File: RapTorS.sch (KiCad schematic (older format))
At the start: 23 parts, among them J1 TestPoint, J2 TestPoint, J3 TestPoint, J4 TestPoint, J5 TestPoint

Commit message: annotate schematic
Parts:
- removed C?: C, symbol RapTorS-rescue:C-device
- gave numbers to parts that had none: 16
- renumbered 0.1uF to 0.1uF1

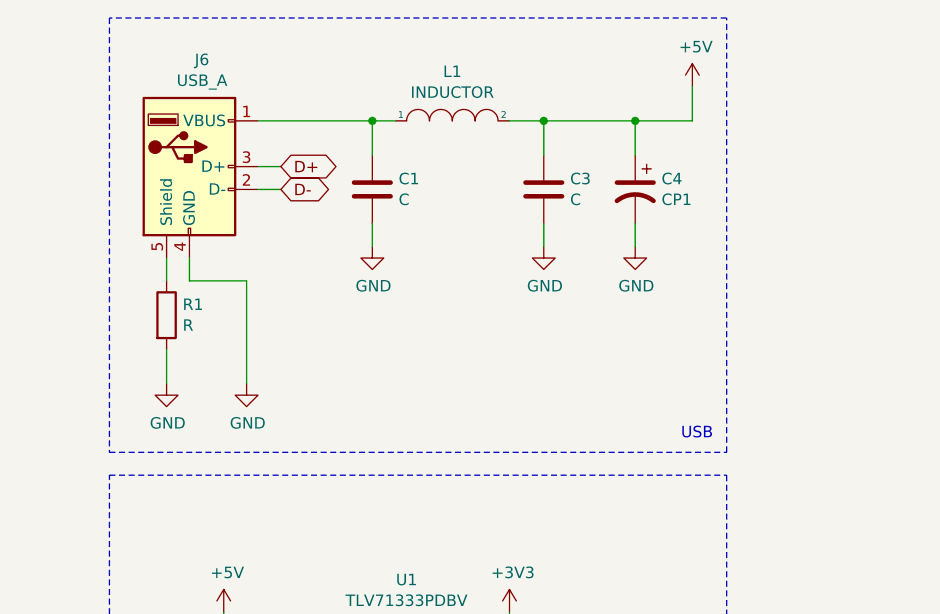
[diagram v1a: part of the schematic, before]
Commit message: set values for USB block
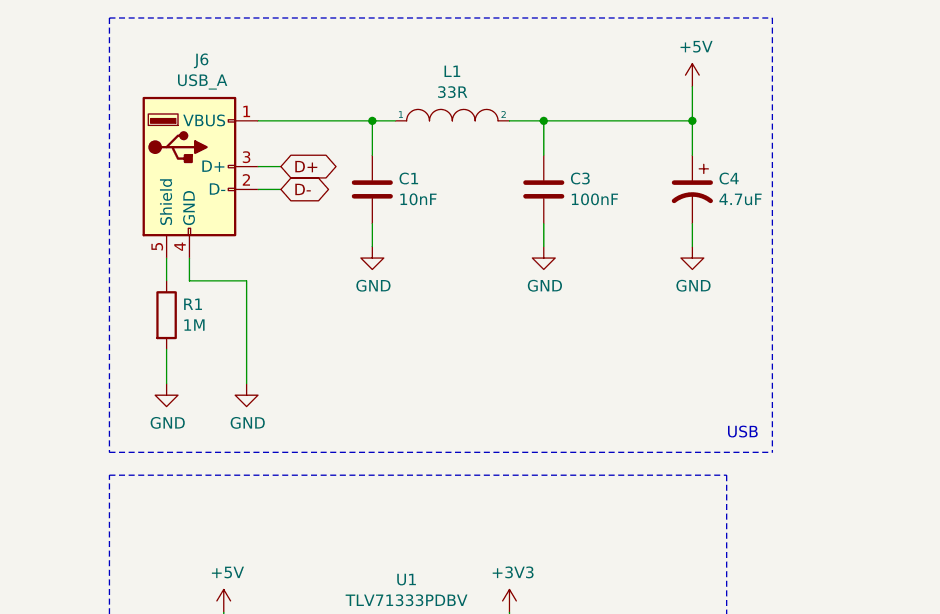
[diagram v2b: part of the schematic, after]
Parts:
- C1: value C -> 10nF
- C3: value C -> 100nF
- C4: value CP1 -> 4.7uF
- L1: value INDUCTOR -> 33R; footprint (none) -> Inductors_SMD:L_0805; Comment (none) -> Ferrite bead
- R1: value R -> 1M; footprint (none) -> Resistors_SMD:R_0805
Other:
- moved on the sheet: C4
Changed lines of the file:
@@
 P 2900 1550
 F 0 "C3" H 3015 1596 50  0000 L CNN
-F 1 "C" H 3015 1505 50  0000 L CNN
+F 1 "100nF" H 3015 1505 50  0000 L CNN
 F 2 "" H 2938 1400 50  0001 C CNN
 F 3 "" H 2900 1550 50  0001 C CNN
@@
 P 1250 2100
 F 0 "R1" H 1320 2146 50  0000 L CNN
-F 1 "R" H 1320 2055 50  0000 L CNN
-F 2 "" V 1180 2100 50  0001 C CNN
+F 1 "1M" H 1320 2055 50  0000 L CNN
+F 2 "Resistors_SMD:R_0805" V 1180 2100 50  0001 C CNN
 F 3 "" H 1250 2100 50  0001 C CNN
 	1    1250 2100
@@
 P 2500 1250
 F 0 "L1" H 2500 1465 50  0000 C CNN
-F 1 "INDUCTOR" H 2500 1374 50  0000 C CNN
-F 2 "" H 2500 1250 50  0001 C CNN
+F 1 "33R" H 2500 1374 50  0000 C CNN
+F 2 "Inductors_SMD:L_0805" H 2500 1250 50  0001 C CNN
 F 3 "" H 2500 1250 50  0001 C CNN
+F 4 "Ferrite bead" H 2500 1250 50  0001 C CNN "Comment"
 	1    2500 1250
 	1    0    0    -1
@@
 P 2150 1550
 F 0 "C1" H 2265 1596 50  0000 L CNN
-F 1 "C" H 2265 1505 50  0000 L CNN
+F 1 "10nF" H 2265 1505 50  0000 L CNN
 F 2 "" H 2188 1400 50  0001 C CNN
 F 3 "" H 2150 1550 50  0001 C CNN
@@
 L RapTorS-rescue:CP1-device C4
 U 1 1 5B63038C
-P 3300 1550
-F 0 "C4" H 3185 1596 50  0000 R CNN
-F 1 "CP1" H 3185 1505 50  0000 R CNN
-F 2 "" H 3300 1550 50  0001 C CNN
-F 3 "" H 3300 1550 50  0001 C CNN
-	1    3300 1550
+P 3550 1550
+F 0 "C4" H 3435 1596 50  0000 R CNN
+F 1 "4.7uF" H 3435 1505 50  0000 R CNN
+F 2 "" H 3550 1550 50  0001 C CNN
+F 3 "" H 3550 1550 50  0001 C CNN
+	1    3550 1550
 	-1   0    0    -1
 $EndComp
@@
 	2900 1250 2900 1400
 Wire Wire Line
-	2900 1250 3300 1250
-Wire Wire Line
-	3300 1250 3300 1400
+	2900 1250 3550 1250
+Wire Wire Line
+	3550 1250 3550 1400
 Connection ~ 2900 1250
 $Comp
@@
 Wire Wire Line
 	3550 1100 3550 1250
-Wire Wire Line
-	3550 1250 3300 1250
-Connection ~ 3300 1250
+Connection ~ 3550 1250
 $Comp
 L power:GND #PWR06
@@
 L power:GND #PWR012
 U 1 1 5B63068F
-P 3300 1800
-F 0 "#PWR012" H 3300 1550 50  0001 C CNN
-F 1 "GND" H 3305 1627 50  0000 C CNN
-F 2 "" H 3300 1800 50  0001 C CNN
-F 3 "" H 3300 1800 50  0001 C CNN
-	1    3300 1800
+P 3550 1800
+F 0 "#PWR012" H 3550 1550 50  0001 C CNN
+F 1 "GND" H 3555 1627 50  0000 C CNN
+F 2 "" H 3550 1800 50  0001 C CNN
+F 3 "" H 3550 1800 50  0001 C CNN
+	1    3550 1800
 	1    0    0    -1
 $EndComp
@@
 	2900 1700 2900 1800
 Wire Wire Line
-	3300 1700 3300 1800
+	3550 1700 3550 1800
 $Comp
 L power:GND #PWR01
@@
 D-
 Wire Notes Line
-	1000 2700 3700 2700
-Wire Notes Line
-	3700 2700 3700 800
-Wire Notes Line
-	3700 800  1000 800
-Wire Notes Line
 	1000 800  1000 2700
-Text Notes 3500 2650 0    50   ~ 0
+Text Notes 3700 2650 0    50   ~ 0
 USB
 $Comp
@@
 Text Notes 5850 4600 0    50   ~ 0
 PROG
+Wire Notes Line
+	3900 800  3900 2700
+Wire Notes Line
+	1000 2700 3900 2700
+Wire Notes Line
+	1000 800  3900 800
 $EndSCHEMATC

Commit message: set values for CPU block
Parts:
- C5: value C -> 100nF; footprint (none) -> Capacitors_SMD:C_0805
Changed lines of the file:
@@
 P 5400 1700
 F 0 "C5" H 5515 1746 50  0000 L CNN
-F 1 "C" H 5515 1655 50  0000 L CNN
-F 2 "" H 5438 1550 50  0001 C CNN
+F 1 "100nF" H 5515 1655 50  0000 L CNN
+F 2 "Capacitors_SMD:C_0805" H 5438 1550 50  0001 C CNN
 F 3 "" H 5400 1700 50  0001 C CNN
 	1    5400 1700

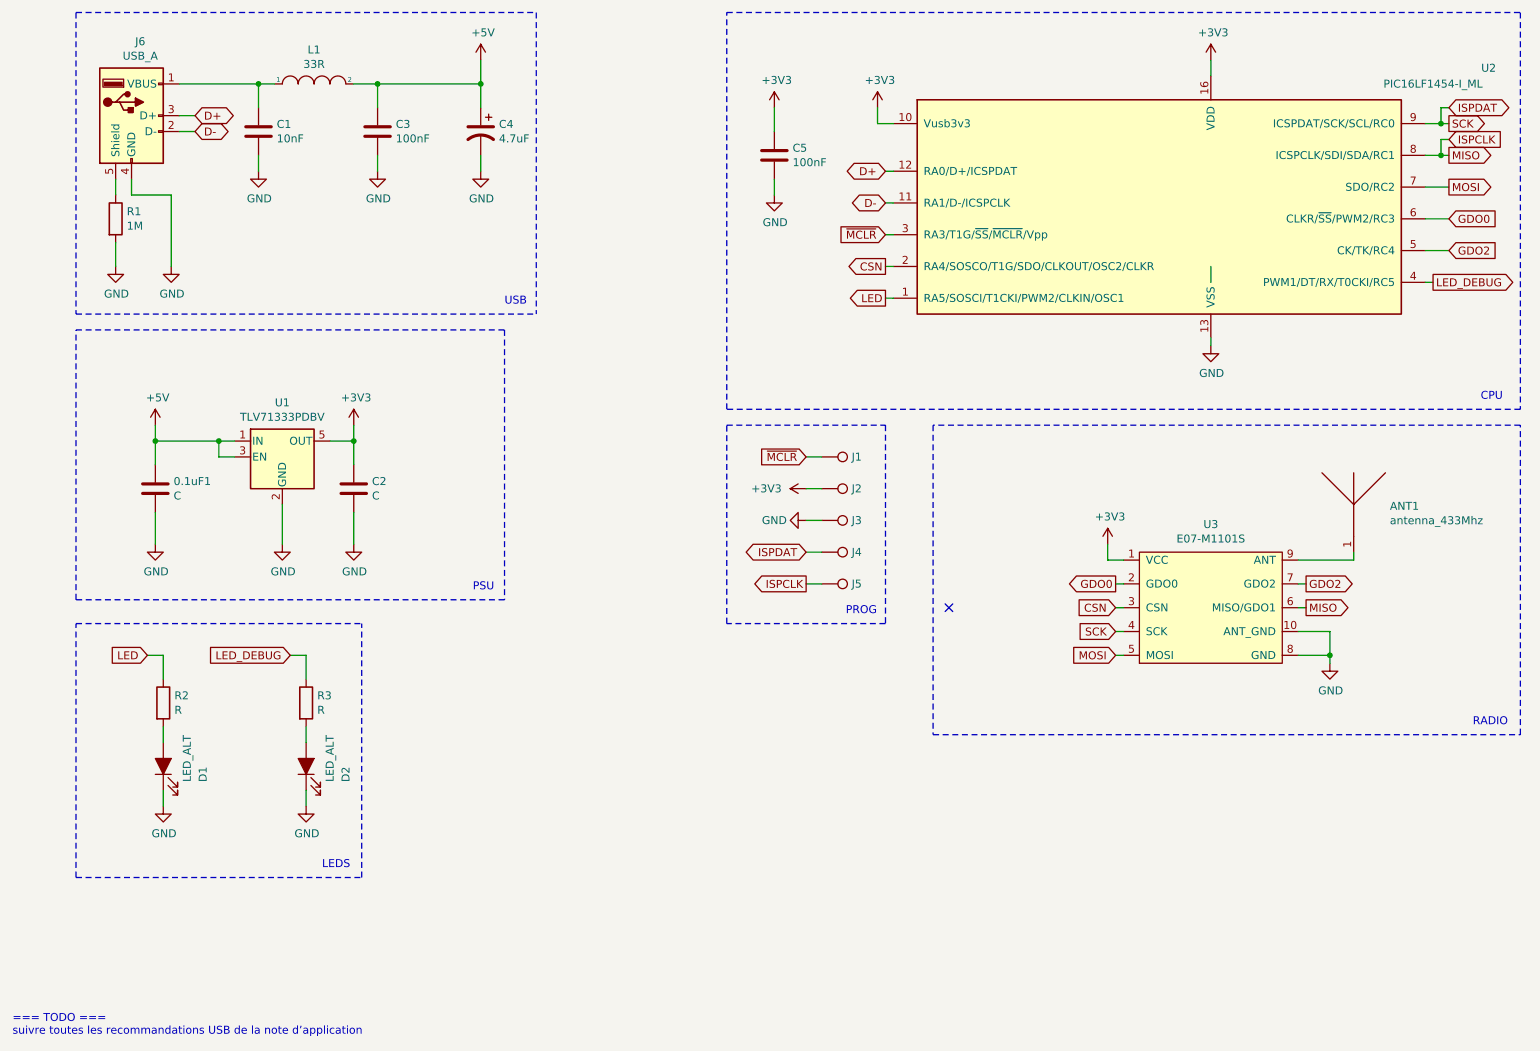
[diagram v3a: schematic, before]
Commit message: set values for PSU block
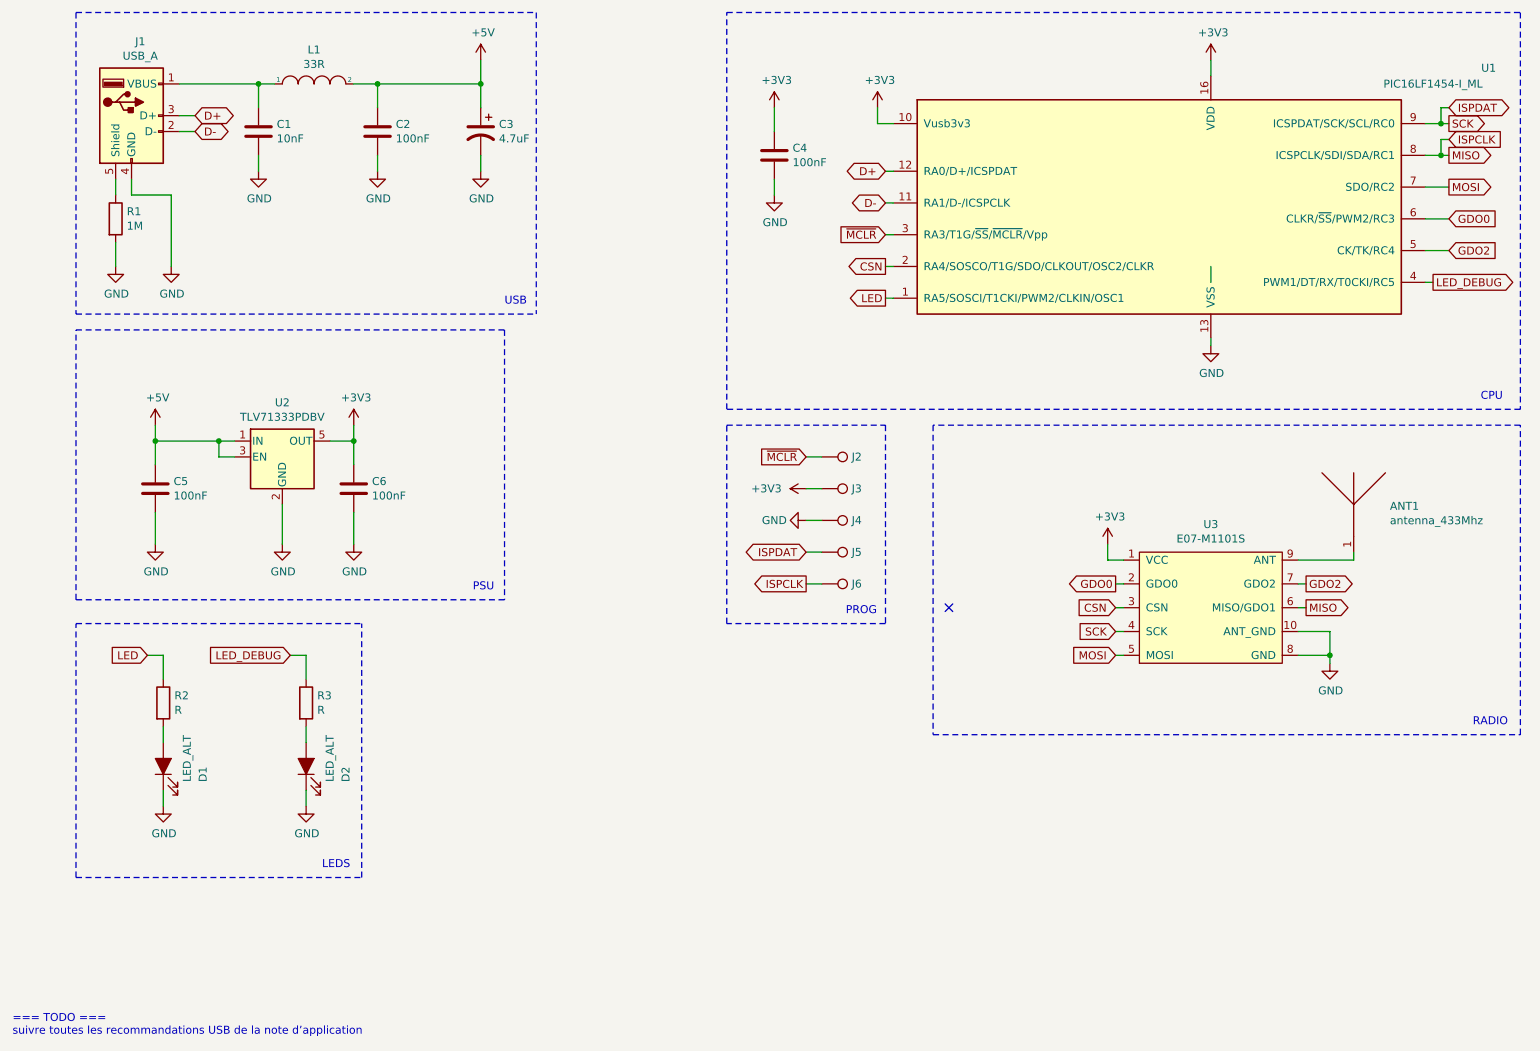
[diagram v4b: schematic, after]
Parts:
- C5: renamed from 0.1uF1; value C -> 100nF; footprint (none) -> Capacitors_SMD:C_0805
- C6: renamed from C2; value C -> 100nF; footprint (none) -> Capacitors_SMD:C_0805
- renumbered C3 to C2, C4 to C3, C5 to C4, J6 to J1, J1 to J2, J2 to J3, J3 to J4, J4 to J5, J5 to J6, U2 to U1, U1 to U2
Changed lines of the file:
@@
 $EndComp
 $Comp
-L Connector:USB_A J6
+L Connector:USB_A J1
 U 1 1 5B61E2AD
 P 1350 1450
-F 0 "J6" H 1405 1917 50  0000 C CNN
+F 0 "J1" H 1405 1917 50  0000 C CNN
 F 1 "USB_A" H 1405 1826 50  0000 C CNN
 F 2 "" H 1500 1400 50  0001 C CNN
@@
 $EndComp
 $Comp
-L RapTorS-rescue:C-device C3
+L RapTorS-rescue:C-device C2
 U 1 1 5B62F72B
 P 2900 1550
-F 0 "C3" H 3015 1596 50  0000 L CNN
+F 0 "C2" H 3015 1596 50  0000 L CNN
 F 1 "100nF" H 3015 1505 50  0000 L CNN
 F 2 "" H 2938 1400 50  0001 C CNN
@@
 $EndComp
 $Comp
-L RapTorS-rescue:C-device 0.1uF1
+L RapTorS-rescue:C-device C5
 U 1 1 5B62F7D7
 P 1500 3800
-F 0 "0.1uF1" H 1615 3846 50  0000 L CNN
-F 1 "C" H 1615 3755 50  0000 L CNN
-F 2 "" H 1538 3650 50  0001 C CNN
+F 0 "C5" H 1615 3846 50  0000 L CNN
+F 1 "100nF" H 1615 3755 50  0000 L CNN
+F 2 "Capacitors_SMD:C_0805" H 1538 3650 50  0001 C CNN
 F 3 "" H 1500 3800 50  0001 C CNN
 	1    1500 3800
@@
 $EndComp
 $Comp
-L RapTorS-rescue:C-device C5
+L RapTorS-rescue:C-device C4
 U 1 1 5B62FCC2
 P 5400 1700
-F 0 "C5" H 5515 1746 50  0000 L CNN
+F 0 "C4" H 5515 1746 50  0000 L CNN
 F 1 "100nF" H 5515 1655 50  0000 L CNN
 F 2 "Capacitors_SMD:C_0805" H 5438 1550 50  0001 C CNN
@@
 $EndComp
 $Comp
-L RapTorS-rescue:CP1-device C4
+L RapTorS-rescue:CP1-device C3
 U 1 1 5B63038C
 P 3550 1550
-F 0 "C4" H 3435 1596 50  0000 R CNN
+F 0 "C3" H 3435 1596 50  0000 R CNN
 F 1 "4.7uF" H 3435 1505 50  0000 R CNN
 F 2 "" H 3550 1550 50  0001 C CNN
@@
 Connection ~ 2900 1250
 $Comp
-L power:+5V #PWR013
+L power:+5V #PWR01
 U 1 1 5B630486
 P 3550 1100
-F 0 "#PWR013" H 3550 950 50  0001 C CNN
+F 0 "#PWR01" H 3550 950 50  0001 C CNN
 F 1 "+5V" H 3565 1273 50  0000 C CNN
 F 2 "" H 3550 1100 50  0001 C CNN
@@
 Connection ~ 3550 1250
 $Comp
-L power:GND #PWR06
+L power:GND #PWR05
 U 1 1 5B630631
 P 2150 1800
-F 0 "#PWR06" H 2150 1550 50  0001 C CNN
+F 0 "#PWR05" H 2150 1550 50  0001 C CNN
 F 1 "GND" H 2155 1627 50  0000 C CNN
 F 2 "" H 2150 1800 50  0001 C CNN
@@
 $EndComp
 $Comp
-L power:GND #PWR011
+L power:GND #PWR06
 U 1 1 5B63066A
 P 2900 1800
-F 0 "#PWR011" H 2900 1550 50  0001 C CNN
+F 0 "#PWR06" H 2900 1550 50  0001 C CNN
 F 1 "GND" H 2905 1627 50  0000 C CNN
 F 2 "" H 2900 1800 50  0001 C CNN
@@
 $EndComp
 $Comp
-L power:GND #PWR012
+L power:GND #PWR07
 U 1 1 5B63068F
 P 3550 1800
-F 0 "#PWR012" H 3550 1550 50  0001 C CNN
+F 0 "#PWR07" H 3550 1550 50  0001 C CNN
 F 1 "GND" H 3555 1627 50  0000 C CNN
 F 2 "" H 3550 1800 50  0001 C CNN
@@
 	3550 1700 3550 1800
 $Comp
-L power:GND #PWR01
+L power:GND #PWR09
 U 1 1 5B63081F
 P 1250 2400
-F 0 "#PWR01" H 1250 2150 50  0001 C CNN
+F 0 "#PWR09" H 1250 2150 50  0001 C CNN
 F 1 "GND" H 1255 2227 50  0000 C CNN
 F 2 "" H 1250 2400 50  0001 C CNN
@@
 	1250 2250 1250 2400
 $Comp
-L power:GND #PWR05
+L power:GND #PWR010
 U 1 1 5B6309AF
 P 1600 2400
-F 0 "#PWR05" H 1600 2150 50  0001 C CNN
+F 0 "#PWR010" H 1600 2150 50  0001 C CNN
 F 1 "GND" H 1605 2227 50  0000 C CNN
 F 2 "" H 1600 2400 50  0001 C CNN
@@
 USB
 $Comp
-L power:GND #PWR015
+L power:GND #PWR08
 U 1 1 5B632473
 P 5400 1950
-F 0 "#PWR015" H 5400 1700 50  0001 C CNN
+F 0 "#PWR08" H 5400 1700 50  0001 C CNN
 F 1 "GND" H 5405 1777 50  0000 C CNN
 F 2 "" H 5400 1950 50  0001 C CNN
@@
 	9600 1500 9650 1500
 $Comp
-L RapTorS-rescue:TLV71333PDBV-regul U1
+L RapTorS-rescue:TLV71333PDBV-regul U2
 U 1 1 5B6396D9
 P 2300 3600
-F 0 "U1" H 2300 3942 50  0000 C CNN
+F 0 "U2" H 2300 3942 50  0000 C CNN
 F 1 "TLV71333PDBV" H 2300 3851 50  0000 C CNN
 F 2 "TO_SOT_Packages_SMD:SOT-23-5" H 2300 3925 50  0001 C CIN
@@
 $EndComp
 $Comp
-L power:GND #PWR07
+L power:GND #PWR017
 U 1 1 5B68188F
 P 2300 4150
-F 0 "#PWR07" H 2300 3900 50  0001 C CNN
+F 0 "#PWR017" H 2300 3900 50  0001 C CNN
 F 1 "GND" H 2305 3977 50  0000 C CNN
 F 2 "" H 2300 4150 50  0001 C CNN
@@
 $EndComp
 $Comp
-L power:GND #PWR03
+L power:GND #PWR016
 U 1 1 5B6818B6
 P 1500 4150
-F 0 "#PWR03" H 1500 3900 50  0001 C CNN
+F 0 "#PWR016" H 1500 3900 50  0001 C CNN
 F 1 "GND" H 1505 3977 50  0000 C CNN
 F 2 "" H 1500 4150 50  0001 C CNN
@@
 	2300 4150 2300 3900
 $Comp
-L power:+5V #PWR02
+L power:+5V #PWR012
 U 1 1 5B683BB0
 P 1500 3400
-F 0 "#PWR02" H 1500 3250 50  0001 C CNN
+F 0 "#PWR012" H 1500 3250 50  0001 C CNN
 F 1 "+5V" H 1515 3573 50  0000 C CNN
 F 2 "" H 1500 3400 50  0001 C CNN
@@
 Connection ~ 1500 3500
 $Comp
-L RapTorS-rescue:C-device C2
+L RapTorS-rescue:C-device C6
 U 1 1 5B684462
 P 2750 3800
-F 0 "C2" H 2865 3846 50  0000 L CNN
-F 1 "C" H 2865 3755 50  0000 L CNN
-F 2 "" H 2788 3650 50  0001 C CNN
+F 0 "C6" H 2865 3846 50  0000 L CNN
+F 1 "100nF" H 2865 3755 50  0000 L CNN
+F 2 "Capacitors_SMD:C_0805" H 2788 3650 50  0001 C CNN
 F 3 "" H 2750 3800 50  0001 C CNN
 	1    2750 3800
@@
 	2750 3500 2750 3650
 $Comp
-L power:GND #PWR010
+L power:GND #PWR018
 U 1 1 5B684DFE
 P 2750 4150
-F 0 "#PWR010" H 2750 3900 50  0001 C CNN
+F 0 "#PWR018" H 2750 3900 50  0001 C CNN
 F 1 "GND" H 2755 3977 50  0000 C CNN
 F 2 "" H 2750 4150 50  0001 C CNN
@@
 	2750 4150 2750 3950
 $Comp
-L power:+3V3 #PWR09
+L power:+3V3 #PWR013
 U 1 1 5B685845
 P 2750 3400
-F 0 "#PWR09" H 2750 3250 50  0001 C CNN
+F 0 "#PWR013" H 2750 3250 50  0001 C CNN
 F 1 "+3V3" H 2765 3573 50  0000 C CNN
 F 2 "" H 2750 3400 50  0001 C CNN
@@
 PSU
 $Comp
-L power:+3V3 #PWR020
+L power:+3V3 #PWR02
 U 1 1 5B68889A
 P 8150 1100
-F 0 "#PWR020" H 8150 950 50  0001 C CNN
+F 0 "#PWR02" H 8150 950 50  0001 C CNN
 F 1 "+3V3" H 8165 1273 50  0000 C CNN
 F 2 "" H 8150 1100 50  0001 C CNN
@@
 	8150 1200 8150 1100
 $Comp
-L power:+3V3 #PWR018
+L power:+3V3 #PWR04
 U 1 1 5B690926
 P 6050 1400
-F 0 "#PWR018" H 6050 1250 50  0001 C CNN
+F 0 "#PWR04" H 6050 1250 50  0001 C CNN
 F 1 "+3V3" H 6065 1573 50  0000 C CNN
 F 2 "" H 6050 1400 50  0001 C CNN
@@
 	6050 1500 6050 1400
 $Comp
-L power:+3V3 #PWR014
+L power:+3V3 #PWR03
 U 1 1 5B69130A
 P 5400 1400
-F 0 "#PWR014" H 5400 1250 50  0001 C CNN
+F 0 "#PWR03" H 5400 1250 50  0001 C CNN
 F 1 "+3V3" H 5415 1573 50  0000 C CNN
 F 2 "" H 5400 1400 50  0001 C CNN
@@
 	5400 1400 5400 1550
 $Comp
-L power:GND #PWR021
+L power:GND #PWR011
 U 1 1 5B6928F4
 P 8150 2900
-F 0 "#PWR021" H 8150 2650 50  0001 C CNN
+F 0 "#PWR011" H 8150 2650 50  0001 C CNN
 F 1 "GND" H 8155 2727 50  0000 C CNN
 F 2 "" H 8150 2900 50  0001 C CNN
@@
 	9050 4250 9050 4200
 $Comp
-L power:GND #PWR022
+L power:GND #PWR020
 U 1 1 5B7BD2F4
 P 8900 4900
-F 0 "#PWR022" H 8900 4650 50  0001 C CNN
+F 0 "#PWR020" H 8900 4650 50  0001 C CNN
 F 1 "GND" H 8905 4727 50  0000 C CNN
 F 2 "" H 8900 4900 50  0001 C CNN
@@
 	7550 4550 7600 4550
 $Comp
-L RapTorS-rescue:PIC16(L)F1454-I_ML-MCU_Microchip_PIC16 U2
+L RapTorS-rescue:PIC16(L)F1454-I_ML-MCU_Microchip_PIC16 U1
 U 1 1 5B5A1512
 P 8150 1800
-F 0 "U2" H 9900 2450 50  0000 C CNN
+F 0 "U1" H 9900 2450 50  0000 C CNN
 F 1 "PIC16LF1454-I_ML" H 9550 2350 50  0000 C CNN
 F 2 "" H 8150 1800 50  0001 C CNN
@@
 	1550 5300 1550 5400
 $Comp
-L power:GND #PWR04
+L power:GND #PWR021
 U 1 1 5B7E3160
 P 1550 5800
-F 0 "#PWR04" H 1550 5550 50  0001 C CNN
+F 0 "#PWR021" H 1550 5550 50  0001 C CNN
 F 1 "GND" H 1555 5627 50  0000 C CNN
 F 2 "" H 1550 5800 50  0001 C CNN
@@
 	2450 5300 2450 5400
 $Comp
-L power:GND #PWR08
+L power:GND #PWR022
 U 1 1 5B7DCAED
 P 2450 5800
-F 0 "#PWR08" H 2450 5550 50  0001 C CNN
+F 0 "#PWR022" H 2450 5550 50  0001 C CNN
 F 1 "GND" H 2455 5627 50  0000 C CNN
 F 2 "" H 2450 5800 50  0001 C CNN
@@
 	1000 6250 2800 6250
 $Comp
-L Connector:TestPoint J1
+L Connector:TestPoint J2
 U 1 1 5B7D9504
 P 5700 3600
-F 0 "J1" V 5700 3787 50  0000 L CNN
+F 0 "J2" V 5700 3787 50  0000 L CNN
 F 1 "TestPoint" V 5745 3788 50  0001 L CNN
 F 2 "" H 5900 3600 50  0001 C CNN
@@
 $EndComp
 $Comp
-L Connector:TestPoint J2
+L Connector:TestPoint J3
 U 1 1 5B7D95BB
 P 5700 3800
-F 0 "J2" V 5700 3987 50  0000 L CNN
+F 0 "J3" V 5700 3987 50  0000 L CNN
 F 1 "TestPoint" V 5745 3988 50  0001 L CNN
 F 2 "" H 5900 3800 50  0001 C CNN
@@
 $EndComp
 $Comp
-L Connector:TestPoint J3
+L Connector:TestPoint J4
 U 1 1 5B7D9654
 P 5700 4000
-F 0 "J3" V 5700 4187 50  0000 L CNN
+F 0 "J4" V 5700 4187 50  0000 L CNN
 F 1 "TestPoint" V 5745 4188 50  0001 L CNN
 F 2 "" H 5900 4000 50  0001 C CNN
@@
 $EndComp
 $Comp
-L Connector:TestPoint J4
+L Connector:TestPoint J5
 U 1 1 5B7D969E
 P 5700 4200
-F 0 "J4" V 5700 4387 50  0000 L CNN
+F 0 "J5" V 5700 4387 50  0000 L CNN
 F 1 "TestPoint" V 5745 4388 50  0001 L CNN
 F 2 "" H 5900 4200 50  0001 C CNN
@@
 $EndComp
 $Comp
-L Connector:TestPoint J5
+L Connector:TestPoint J6
 U 1 1 5B7D96DD
 P 5700 4400
-F 0 "J5" V 5700 4587 50  0000 L CNN
+F 0 "J6" V 5700 4587 50  0000 L CNN
 F 1 "TestPoint" V 5745 4588 50  0001 L CNN
 F 2 "" H 5900 4400 50  0001 C CNN
@@
 ~MCLR
 $Comp
-L power:+3V3 #PWR016
+L power:+3V3 #PWR014
 U 1 1 5B7D9D26
 P 5600 3800
-F 0 "#PWR016" H 5600 3650 50  0001 C CNN
+F 0 "#PWR014" H 5600 3650 50  0001 C CNN
 F 1 "+3V3" V 5600 4050 50  0000 C CNN
 F 2 "" H 5600 3800 50  0001 C CNN
@@
 $EndComp
 $Comp
-L power:GND #PWR017
+L power:GND #PWR015
 U 1 1 5B7D9D5F
 P 5600 4000
-F 0 "#PWR017" H 5600 3750 50  0001 C CNN
+F 0 "#PWR015" H 5600 3750 50  0001 C CNN
 F 1 "GND" V 5600 3800 50  0000 C CNN
 F 2 "" H 5600 4000 50  0001 C CNN
